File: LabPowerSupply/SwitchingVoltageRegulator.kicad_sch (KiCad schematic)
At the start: 14 parts

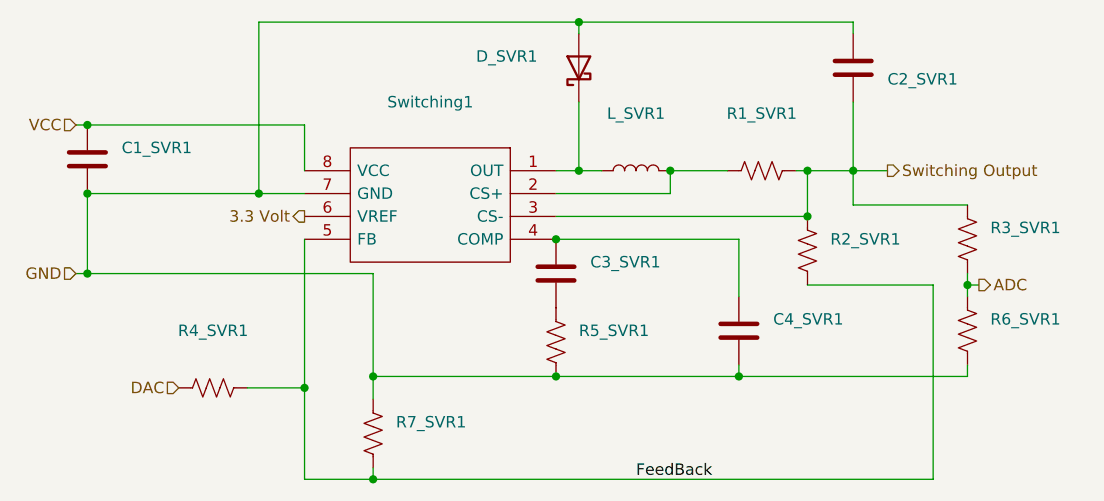
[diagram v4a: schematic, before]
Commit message: Added mcu capacitors, split 5v inductors
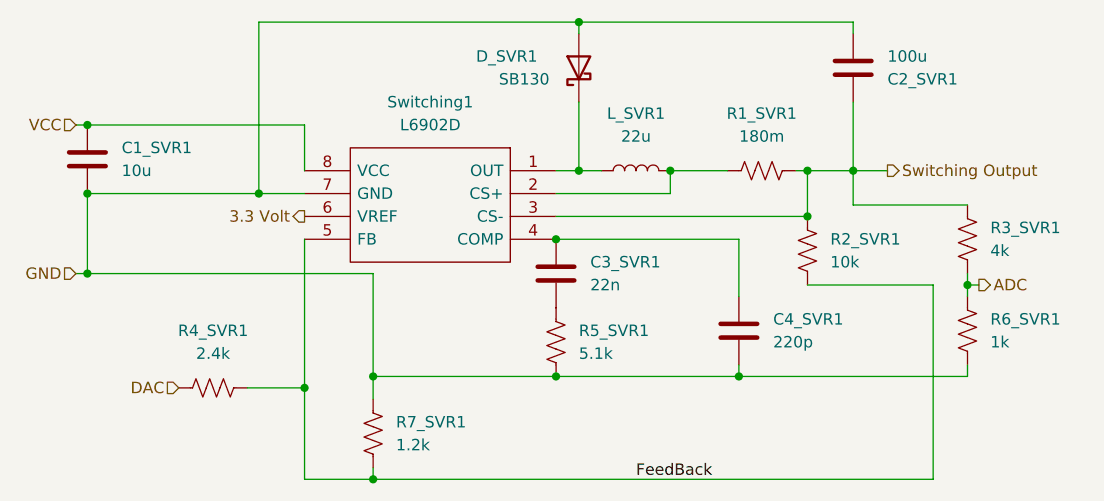
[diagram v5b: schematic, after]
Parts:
- C1_SVR1: value (none) -> 10u; footprint (none) -> Capacitor_THT:C_Disc_D5.0mm_W2.5mm_P2.50mm
- C2_SVR1: value (none) -> 100u; footprint (none) -> Capacitor_THT:C_Radial_D8.0mm_H7.0mm_P3.50mm
- C3_SVR1: value (none) -> 22n; footprint (none) -> Capacitor_THT:C_Disc_D7.0mm_W2.5mm_P5.00mm
- C4_SVR1: value (none) -> 220p; footprint (none) -> Capacitor_THT:C_Disc_D7.5mm_W2.5mm_P5.00mm
- D_SVR1: value (none) -> SB130; footprint (none) -> Diode_THT:D_DO-41_SOD81_P10.16mm_Horizontal
- L_SVR1: value (none) -> 22u; footprint (none) -> Inductor_THT:L_Radial_D6.0mm_P4.00mm
- R1_SVR1: value (none) -> 180m; footprint (none) -> Resistor_SMD:R_0603_1608Metric
- R2_SVR1: value (none) -> 10k; footprint (none) -> Resistor_SMD:R_0603_1608Metric
- R3_SVR1: value (none) -> 4k; footprint (none) -> Resistor_SMD:R_0603_1608Metric
- R4_SVR1: value (none) -> 2.4k; footprint (none) -> Resistor_SMD:R_0603_1608Metric
- R5_SVR1: value (none) -> 5.1k; footprint (none) -> Resistor_SMD:R_0603_1608Metric
- R6_SVR1: value (none) -> 1k; footprint (none) -> Resistor_SMD:R_0603_1608Metric
- R7_SVR1: value (none) -> 1.2k; footprint (none) -> Resistor_SMD:R_0603_1608Metric
- Switching1: value (none) -> L6902D; footprint (none) -> Package_SO:SOIC-8-1EP_3.9x4.9mm_P1.27mm_EP2.95x4.9mm_Mask2.71x3.4mm
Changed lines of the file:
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@@
       (effects (font (size 1.27 1.27)) (justify left))
     )
-    (property "Value" "" (id 1) (at 120.65 123.1899 0)
-      (effects (font (size 1.27 1.27)) (justify left))
-    )
-    (property "Footprint" "" (id 2) (at 119.126 122.174 90)
+    (property "Value" "1.2k" (id 1) (at 120.65 123.1899 0)
+      (effects (font (size 1.27 1.27)) (justify left))
+    )
+    (property "Footprint" "Resistor_SMD:R_0603_1608Metric" (id 2) (at 119.126 122.174 90)
       (effects (font (size 1.27 1.27)) hide)
     )
@@
     (in_bom yes) (on_board yes) (fields_autoplaced)
     (property "Reference" "R1_SVR1" (id 0) (at 161.29 86.36 90))
-    (property "Value" "" (id 1) (at 161.29 88.9 90))
-    (property "Footprint" "" (id 2) (at 161.544 91.694 90)
+    (property "Value" "180m" (id 1) (at 161.29 88.9 90))
+    (property "Footprint" "Resistor_SMD:R_0603_1608Metric" (id 2) (at 161.544 91.694 90)
       (effects (font (size 1.27 1.27)) hide)
     )
@@
       (effects (font (size 1.27 1.27)) (justify right))
     )
-    (property "Value" "" (id 1) (at 132.08 82.55 90)
+    (property "Value" "SB130" (id 1) (at 132.08 82.55 90)
       (effects (font (size 1.27 1.27)) (justify right))
     )
-    (property "Footprint" "" (id 2) (at 145.415 81.28 0)
+    (property "Footprint" "Diode_THT:D_DO-41_SOD81_P10.16mm_Horizontal" (id 2) (at 145.415 81.28 0)
       (effects (font (size 1.27 1.27)) hide)
     )
@@
       (effects (font (size 1.27 1.27)) (justify left))
     )
-    (property "Value" "" (id 1) (at 142.24 105.4099 0)
-      (effects (font (size 1.27 1.27)) (justify left))
-    )
-    (property "Footprint" "" (id 2) (at 139.3952 107.95 0)
+    (property "Value" "22n" (id 1) (at 142.24 105.4099 0)
+      (effects (font (size 1.27 1.27)) (justify left))
+    )
+    (property "Footprint" "Capacitor_THT:C_Disc_D7.0mm_W2.5mm_P5.00mm" (id 2) (at 139.3952 107.95 0)
       (effects (font (size 1.27 1.27)) hide)
     )
@@
     (in_bom yes) (on_board yes) (fields_autoplaced)
     (property "Reference" "Switching1" (id 0) (at 124.46 85.09 0))
-    (property "Value" "" (id 1) (at 124.46 87.63 0))
-    (property "Footprint" "" (id 2) (at 114.3 90.17 0)
+    (property "Value" "L6902D" (id 1) (at 124.46 87.63 0))
+    (property "Footprint" "Package_SO:SOIC-8-1EP_3.9x4.9mm_P1.27mm_EP2.95x4.9mm_Mask2.71x3.4mm" (id 2) (at 114.3 90.17 0)
       (effects (font (size 1.27 1.27)) (justify left) hide)
     )
@@
     (in_bom yes) (on_board yes) (fields_autoplaced)
     (property "Reference" "L_SVR1" (id 0) (at 147.32 86.36 90))
-    (property "Value" "" (id 1) (at 147.32 88.9 90))
-    (property "Footprint" "" (id 2) (at 147.32 92.71 0)
+    (property "Value" "22u" (id 1) (at 147.32 88.9 90))
+    (property "Footprint" "Inductor_THT:L_Radial_D6.0mm_P4.00mm" (id 2) (at 147.32 92.71 0)
       (effects (font (size 1.27 1.27)) hide)
     )
@@
     (in_bom yes) (on_board yes) (fields_autoplaced)
     (property "Reference" "R4_SVR1" (id 0) (at 100.33 110.49 90))
-    (property "Value" "" (id 1) (at 100.33 113.03 90))
-    (property "Footprint" "" (id 2) (at 100.076 117.856 90)
+    (property "Value" "2.4k" (id 1) (at 100.33 113.03 90))
+    (property "Footprint" "Resistor_SMD:R_0603_1608Metric" (id 2) (at 100.076 117.856 90)
       (effects (font (size 1.27 1.27)) hide)
     )
@@
       (effects (font (size 1.27 1.27)) (justify left))
     )
-    (property "Value" "" (id 1) (at 186.69 111.7599 0)
-      (effects (font (size 1.27 1.27)) (justify left))
-    )
-    (property "Footprint" "" (id 2) (at 185.166 110.744 90)
+    (property "Value" "1k" (id 1) (at 186.69 111.7599 0)
+      (effects (font (size 1.27 1.27)) (justify left))
+    )
+    (property "Footprint" "Resistor_SMD:R_0603_1608Metric" (id 2) (at 185.166 110.744 90)
       (effects (font (size 1.27 1.27)) hide)
     )
@@
       (effects (font (size 1.27 1.27)) (justify left))
     )
-    (property "Value" "" (id 1) (at 90.17 92.7099 0)
-      (effects (font (size 1.27 1.27)) (justify left))
-    )
-    (property "Footprint" "" (id 2) (at 87.3252 95.25 0)
+    (property "Value" "10u" (id 1) (at 90.17 92.7099 0)
+      (effects (font (size 1.27 1.27)) (justify left))
+    )
+    (property "Footprint" "Capacitor_THT:C_Disc_D5.0mm_W2.5mm_P2.50mm" (id 2) (at 87.3252 95.25 0)
       (effects (font (size 1.27 1.27)) hide)
     )
@@
       (effects (font (size 1.27 1.27)) (justify left))
     )
-    (property "Value" "" (id 1) (at 175.26 80.0101 0)
-      (effects (font (size 1.27 1.27)) (justify left))
-    )
-    (property "Footprint" "" (id 2) (at 172.4152 77.47 0)
+    (property "Value" "100u" (id 1) (at 175.26 80.0101 0)
+      (effects (font (size 1.27 1.27)) (justify left))
+    )
+    (property "Footprint" "Capacitor_THT:C_Radial_D8.0mm_H7.0mm_P3.50mm" (id 2) (at 172.4152 77.47 0)
       (effects (font (size 1.27 1.27)) hide)
     )
@@
       (effects (font (size 1.27 1.27)) (justify left))
     )
-    (property "Value" "" (id 1) (at 186.69 101.5999 0)
-      (effects (font (size 1.27 1.27)) (justify left))
-    )
-    (property "Footprint" "" (id 2) (at 185.166 100.584 90)
+    (property "Value" "4k" (id 1) (at 186.69 101.5999 0)
+      (effects (font (size 1.27 1.27)) (justify left))
+    )
+    (property "Footprint" "Resistor_SMD:R_0603_1608Metric" (id 2) (at 185.166 100.584 90)
       (effects (font (size 1.27 1.27)) hide)
     )
@@
       (effects (font (size 1.27 1.27)) (justify left))
     )
-    (property "Value" "" (id 1) (at 162.56 111.7599 0)
-      (effects (font (size 1.27 1.27)) (justify left))
-    )
-    (property "Footprint" "" (id 2) (at 159.7152 114.3 0)
+    (property "Value" "220p" (id 1) (at 162.56 111.7599 0)
+      (effects (font (size 1.27 1.27)) (justify left))
+    )
+    (property "Footprint" "Capacitor_THT:C_Disc_D7.5mm_W2.5mm_P5.00mm" (id 2) (at 159.7152 114.3 0)
       (effects (font (size 1.27 1.27)) hide)
     )
@@
       (effects (font (size 1.27 1.27)) (justify left))
     )
-    (property "Value" "" (id 1) (at 168.91 102.8699 0)
-      (effects (font (size 1.27 1.27)) (justify left))
-    )
-    (property "Footprint" "" (id 2) (at 167.386 101.854 90)
+    (property "Value" "10k" (id 1) (at 168.91 102.8699 0)
+      (effects (font (size 1.27 1.27)) (justify left))
+    )
+    (property "Footprint" "Resistor_SMD:R_0603_1608Metric" (id 2) (at 167.386 101.854 90)
       (effects (font (size 1.27 1.27)) hide)
     )
@@
       (effects (font (size 1.27 1.27)) (justify left))
     )
-    (property "Value" "" (id 1) (at 140.97 113.0299 0)
-      (effects (font (size 1.27 1.27)) (justify left))
-    )
-    (property "Footprint" "" (id 2) (at 139.446 112.014 90)
-      (effects (font (size 1.27 1.27)) hide)
-    )
+    (property "Value" "5.1k" (id 1) (at 140.97 113.0299 0)
+      (effects (font (size 1.27 1.27)) (justify left))
+    )
+    (property "Footprint" "Resistor_SMD:R_0603_1608Metric" (id 2) (at 139.446 112.014 90)
+      (effects (font (size 1.27 1.27)) hide)
+    )

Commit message: Fixed 5v/3v regulators, fixed switching regulator comp
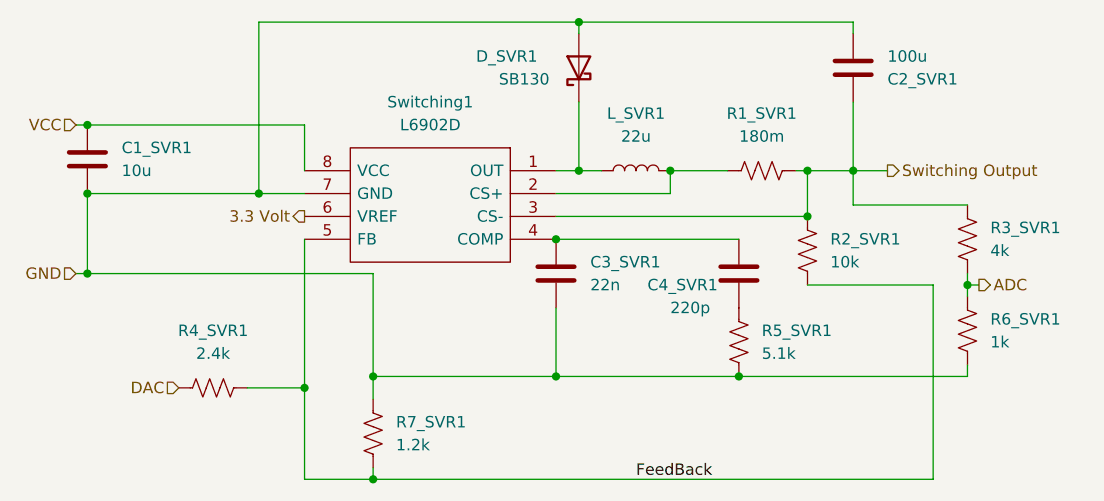
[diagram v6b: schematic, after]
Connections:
- net GND: now also C3_SVR1.2; no longer C4_SVR1.2
- net at R5_SVR1.1: now also C4_SVR1.2; no longer C3_SVR1.2
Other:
- moved on the sheet: C4_SVR1, R5_SVR1
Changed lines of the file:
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@@
   (junction (at 110.49 116.84) (diameter 0) (color 0 0 0 0)
   )
+  (junction (at 138.43 115.57) (diameter 0) (color 0 0 0 0)
+  )
+  (junction (at 151.13 92.71) (diameter 0) (color 0 0 0 0)
+  )
   (junction (at 158.75 115.57) (diameter 0) (color 0 0 0 0)
   )
-  (junction (at 151.13 92.71) (diameter 0) (color 0 0 0 0)
-  )
   (junction (at 138.43 100.33) (diameter 0) (color 0 0 0 0)
   )
@@
   (junction (at 140.97 92.71) (diameter 0) (color 0 0 0 0)
   )
-  (junction (at 138.43 115.57) (diameter 0) (color 0 0 0 0)
-  )
   (junction (at 105.41 95.25) (diameter 0) (color 0 0 0 0)
   )
@@
     (stroke (width 0) (type default) (color 0 0 0 0))
   )
-  (wire (pts (xy 158.75 114.3) (xy 158.75 115.57))
-    (stroke (width 0) (type default) (color 0 0 0 0))
-  )
   (wire (pts (xy 165.1 92.71) (xy 166.37 92.71))
     (stroke (width 0) (type default) (color 0 0 0 0))
@@
     (stroke (width 0) (type default) (color 0 0 0 0))
   )
-  (wire (pts (xy 184.15 115.57) (xy 158.75 115.57))
-    (stroke (width 0) (type default) (color 0 0 0 0))
-  )
   (wire (pts (xy 110.49 116.84) (xy 110.49 127))
     (stroke (width 0) (type default) (color 0 0 0 0))
@@
     (stroke (width 0) (type default) (color 0 0 0 0))
   )
-  (wire (pts (xy 158.75 106.68) (xy 158.75 100.33))
-    (stroke (width 0) (type default) (color 0 0 0 0))
-  )
   (wire (pts (xy 158.75 100.33) (xy 138.43 100.33))
     (stroke (width 0) (type default) (color 0 0 0 0))
@@
     (stroke (width 0) (type default) (color 0 0 0 0))
   )
+  (wire (pts (xy 138.43 107.95) (xy 138.43 115.57))
+    (stroke (width 0) (type default) (color 0 0 0 0))
+  )
   (wire (pts (xy 110.49 87.63) (xy 86.36 87.63))
     (stroke (width 0) (type default) (color 0 0 0 0))
@@
     (stroke (width 0) (type default) (color 0 0 0 0))
   )
+  (wire (pts (xy 158.75 115.57) (xy 184.15 115.57))
+    (stroke (width 0) (type default) (color 0 0 0 0))
+  )
+  (wire (pts (xy 140.97 77.47) (xy 140.97 76.2))
+    (stroke (width 0) (type default) (color 0 0 0 0))
+  )
+  (wire (pts (xy 86.36 95.25) (xy 86.36 104.14))
+    (stroke (width 0) (type default) (color 0 0 0 0))
+  )
+  (wire (pts (xy 110.49 92.71) (xy 110.49 87.63))
+    (stroke (width 0) (type default) (color 0 0 0 0))
+  )
   (wire (pts (xy 138.43 115.57) (xy 158.75 115.57))
-    (stroke (width 0) (type default) (color 0 0 0 0))
-  )
-  (wire (pts (xy 140.97 77.47) (xy 140.97 76.2))
-    (stroke (width 0) (type default) (color 0 0 0 0))
-  )
-  (wire (pts (xy 86.36 95.25) (xy 86.36 104.14))
-    (stroke (width 0) (type default) (color 0 0 0 0))
-  )
-  (wire (pts (xy 110.49 92.71) (xy 110.49 87.63))
     (stroke (width 0) (type default) (color 0 0 0 0))
   )
@@
     (pin "2")
   )
-  (symbol (lib_id "Device:C") (at 158.75 110.49 0) (unit 1)
-    (in_bom yes) (on_board yes) (fields_autoplaced)
-    (property "Reference" "C4_SVR1" (id 0) (at 162.56 109.2199 0)
-      (effects (font (size 1.27 1.27)) (justify left))
-    )
-    (property "Value" "220p" (id 1) (at 162.56 111.7599 0)
-      (effects (font (size 1.27 1.27)) (justify left))
-    )
-    (property "Footprint" "Capacitor_THT:C_Disc_D7.5mm_W2.5mm_P5.00mm" (id 2) (at 159.7152 114.3 0)
-      (effects (font (size 1.27 1.27)) hide)
-    )
-    (property "Datasheet" "~" (id 3) (at 158.75 110.49 0)
+  (symbol (lib_id "Device:C") (at 158.75 104.14 0) (unit 1)
+    (in_bom yes) (on_board yes)
+    (property "Reference" "C4_SVR1" (id 0) (at 148.59 105.41 0)
+      (effects (font (size 1.27 1.27)) (justify left))
+    )
+    (property "Value" "220p" (id 1) (at 151.13 107.95 0)
+      (effects (font (size 1.27 1.27)) (justify left))
+    )
+    (property "Footprint" "Capacitor_THT:C_Disc_D7.5mm_W2.5mm_P5.00mm" (id 2) (at 159.7152 107.95 0)
+      (effects (font (size 1.27 1.27)) hide)
+    )
+    (property "Datasheet" "~" (id 3) (at 158.75 104.14 0)
       (effects (font (size 1.27 1.27)) hide)
     )
@@
     (pin "2")
   )
-  (symbol (lib_id "Device:R_US") (at 138.43 111.76 0) (unit 1)
-    (in_bom yes) (on_board yes) (fields_autoplaced)
-    (property "Reference" "R5_SVR1" (id 0) (at 140.97 110.4899 0)
-      (effects (font (size 1.27 1.27)) (justify left))
-    )
-    (property "Value" "5.1k" (id 1) (at 140.97 113.0299 0)
-      (effects (font (size 1.27 1.27)) (justify left))
-    )
-    (property "Footprint" "Resistor_SMD:R_0603_1608Metric" (id 2) (at 139.446 112.014 90)
-      (effects (font (size 1.27 1.27)) hide)
-    )
-    (property "Datasheet" "~" (id 3) (at 138.43 111.76 0)
-      (effects (font (size 1.27 1.27)) hide)
-    )
+  (symbol (lib_id "Device:R_US") (at 158.75 111.76 0) (unit 1)
+    (in_bom yes) (on_board yes) (fields_autoplaced)
+    (property "Reference" "R5_SVR1" (id 0) (at 161.29 110.4899 0)
+      (effects (font (size 1.27 1.27)) (justify left))
+    )
+    (property "Value" "5.1k" (id 1) (at 161.29 113.0299 0)
+      (effects (font (size 1.27 1.27)) (justify left))
+    )
+    (property "Footprint" "Resistor_SMD:R_0603_1608Metric" (id 2) (at 159.766 112.014 90)
+      (effects (font (size 1.27 1.27)) hide)
+    )
+    (property "Datasheet" "~" (id 3) (at 158.75 111.76 0)
+      (effects (font (size 1.27 1.27)) hide)
+    )

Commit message: another commit
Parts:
- C3_SVR1: footprint Capacitor_THT:C_Disc_D7.0mm_W2.5mm_P5.00mm -> Capacitor_THT:C_Disc_D7.5mm_W2.5mm_P5.00mm
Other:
- moved on the sheet: C3_SVR1
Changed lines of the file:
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@@
+    (stroke (width 0) (type default) (color 0 0 0 0))
+  )
+  (wire (pts (xy 138.43 107.95) (xy 138.43 100.33))
     (stroke (width 0) (type default) (color 0 0 0 0))
   )
@@
   )
   (wire (pts (xy 118.11 125.73) (xy 118.11 127))
-    (stroke (width 0) (type default) (color 0 0 0 0))
-  )
-  (wire (pts (xy 138.43 107.95) (xy 138.43 115.57))
     (stroke (width 0) (type default) (color 0 0 0 0))
   )
@@
     (pin "2")
   )
-  (symbol (lib_id "Device:C") (at 138.43 104.14 0) (unit 1)
-    (in_bom yes) (on_board yes) (fields_autoplaced)
-    (property "Reference" "C3_SVR1" (id 0) (at 142.24 102.8699 0)
-      (effects (font (size 1.27 1.27)) (justify left))
-    )
-    (property "Value" "22n" (id 1) (at 142.24 105.4099 0)
-      (effects (font (size 1.27 1.27)) (justify left))
-    )
-    (property "Footprint" "Capacitor_THT:C_Disc_D7.0mm_W2.5mm_P5.00mm" (id 2) (at 139.3952 107.95 0)
-      (effects (font (size 1.27 1.27)) hide)
-    )
-    (property "Datasheet" "~" (id 3) (at 138.43 104.14 0)
+  (symbol (lib_id "Device:C") (at 138.43 111.76 0) (unit 1)
+    (in_bom yes) (on_board yes) (fields_autoplaced)
+    (property "Reference" "C3_SVR1" (id 0) (at 142.24 110.4899 0)
+      (effects (font (size 1.27 1.27)) (justify left))
+    )
+    (property "Value" "22n" (id 1) (at 142.24 113.0299 0)
+      (effects (font (size 1.27 1.27)) (justify left))
+    )
+    (property "Footprint" "Capacitor_THT:C_Disc_D7.5mm_W2.5mm_P5.00mm" (id 2) (at 139.3952 115.57 0)
+      (effects (font (size 1.27 1.27)) hide)
+    )
+    (property "Datasheet" "~" (id 3) (at 138.43 111.76 0)
       (effects (font (size 1.27 1.27)) hide)
     )
@@
   (symbol (lib_id "Device:C") (at 158.75 104.14 0) (unit 1)
     (in_bom yes) (on_board yes)
-    (property "Reference" "C4_SVR1" (id 0) (at 148.59 105.41 0)
-      (effects (font (size 1.27 1.27)) (justify left))
-    )
-    (property "Value" "220p" (id 1) (at 151.13 107.95 0)
-      (effects (font (size 1.27 1.27)) (justify left))
-    )
+    (property "Reference" "C4_SVR1" (id 0) (at 147.32 102.87 0)
+      (effects (font (size 1.27 1.27)) (justify left))
+    )
+    (property "Value" "220p" (id 1) (at 149.86 105.41 0)
+      (effects (font (size 1.27 1.27)) (justify left))
+    )
